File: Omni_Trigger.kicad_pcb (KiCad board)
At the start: 2 copper layers, 127 x 48 mm, 43 parts, among them J1 Conn_02x13_Top_Bottom, J2 Conn_02x04_Odd_Even, J3 Conn_02x02_Odd_Even, J4 Conn_02x04_Odd_Even, J5 Screw_Terminal_01x08, J6 Screw_Terminal_01x04, J7 Screw_Terminal_01x02, J8 Screw_Terminal_01x02, K1 G5LE-1, K2 G5LE-1, K3 G5LE-1, K4 G5LE-1, Q1 BS170F, Q2 BS170F, Q3 BS170F, Q4 BS170F

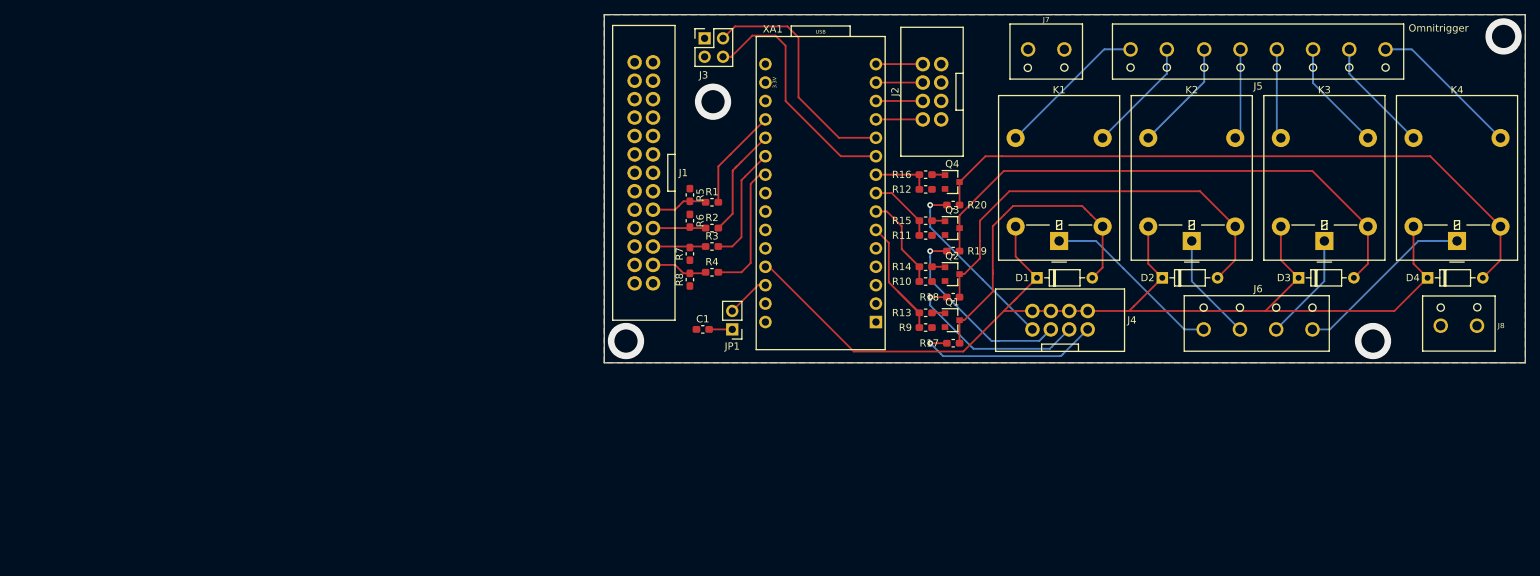
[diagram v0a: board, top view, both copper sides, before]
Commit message: Redrew Board in Stablöe Kicad for compatibility
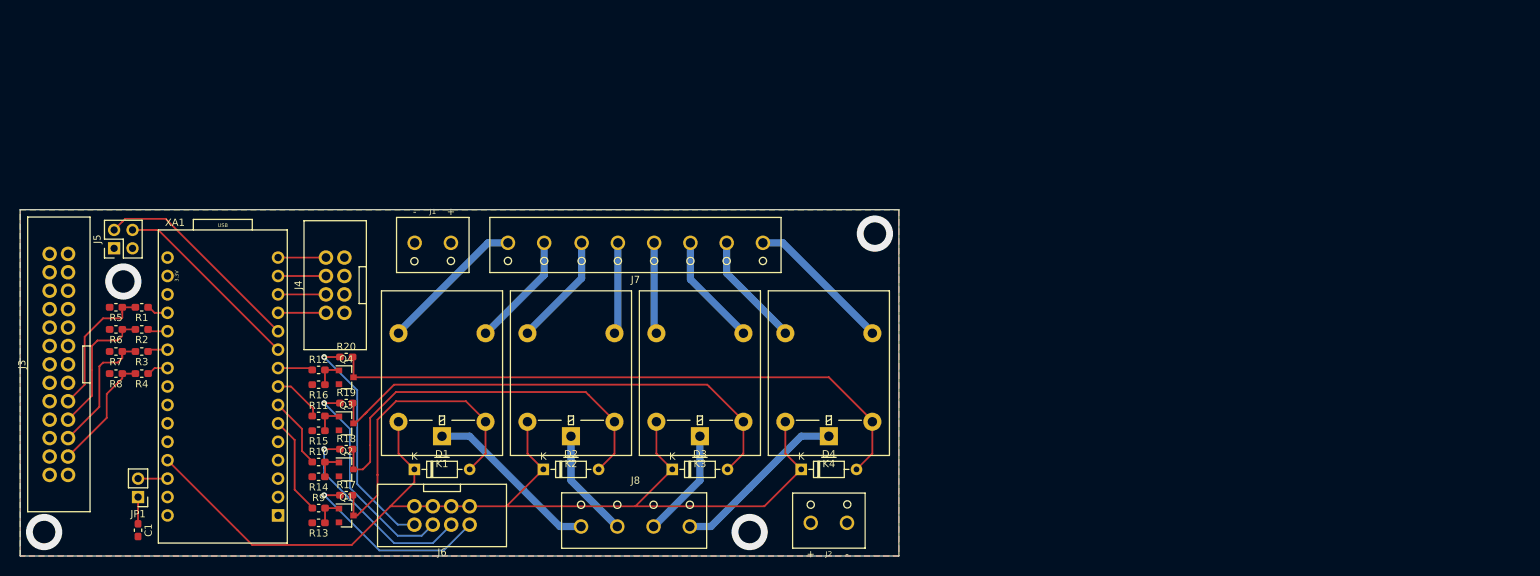
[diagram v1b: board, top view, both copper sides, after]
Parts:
- J1: value Conn_02x13_Top_Bottom -> Screw_Terminal_01x02; footprint IDC:IDC_13x02_Sided -> RS_Screw:RS_Screw_Term_x2
- J2: value Conn_02x04_Odd_Even -> Screw_Terminal_01x02; footprint IDC:IDC_04x02 -> RS_Screw:RS_Screw_Term_x2
- J3: value Conn_02x02_Odd_Even -> Conn_02x13_Top_Bottom; footprint Connector_PinHeader_2.54mm:PinHeader_2x02_P2.54mm_Vertical -> IDC:IDC_13x02_Sided
- J5: value Screw_Terminal_01x08 -> Conn_02x02_Odd_Even; footprint RS_Screw:RS_Screw_Term_x8 -> Connector_PinHeader_2.54mm:PinHeader_2x02_P2.54mm_Vertical
- J6: value Screw_Terminal_01x04 -> Conn_02x04_Odd_Even; footprint RS_Screw:RS_Screw_Term_x4 -> IDC:IDC_04x02
- J7: value Screw_Terminal_01x02 -> Screw_Terminal_01x08; footprint RS_Screw:RS_Screw_Term_x2 -> RS_Screw:RS_Screw_Term_x8
- J8: value Screw_Terminal_01x02 -> Screw_Terminal_01x04; footprint RS_Screw:RS_Screw_Term_x2 -> RS_Screw:RS_Screw_Term_x4
- R1, R13, R14, R15, R16, R2, R3, R4: value 100 -> R
- R10, R11, R12, R5, R6, R7, R8, R9: value 10k -> R
- R17, R18, R19, R20: value 300 -> R
- moved J5 160.1 mm to (42.4, 93.2), turned to 90 degrees
- moved J8 116.9 mm to (114.3, 131.6)
- moved J6 115.4 mm to (87.6, 130.0), turned to 180 degrees
- moved J4 100.1 mm to (72.9, 98.3), turned to 90 degrees
- moved J3 99.7 mm to (34.8, 109.2), turned to 90 degrees
- moved K4 90.7 mm to (141.0, 119.1)
- moved D3 90.3 mm to (119.4, 123.7)
- moved D4 90.3 mm to (137.2, 123.7)
- moved K3 90.2 mm to (123.2, 119.1)
- moved D1 89.8 mm to (83.8, 123.7)
- moved K2 89.7 mm to (105.4, 119.1)
- moved D2 89.3 mm to (101.6, 123.7)
- moved K1 89.2 mm to (87.6, 119.1)
- moved R13 88.6 mm to (70.6, 131.1)
- moved R14 88.6 mm to (70.6, 124.7)
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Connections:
- C1 pad 1: GND -> Net-(C1-Pad1)
- C1 pad 2: Net-(C1-Pad2) -> GND
- J1 pad 1: (no net) -> /Shield
- J1 pad 2: Net-(J1-Pad2) -> /Shield
- J2 pad 1: GND -> /Shield
- J2 pad 2: Net-(J2-Pad2) -> /Shield
- J3 pad 1: GND -> Net-(J3-Pad1)
- J3 pad 3: GND -> Net-(J3-Pad3)
- J4 pad 1: Net-(J4-Pad1) -> GND
- J4 pad 2: +5V -> Net-(J4-Pad2)
- J4 pad 3: Net-(J4-Pad3) -> GND
- J4 pad 4: +5V -> Net-(J4-Pad4)
- J4 pad 5: Net-(J4-Pad5) -> GND
- J4 pad 6: +5V -> Net-(J4-Pad6)
- J4 pad 7: Net-(J4-Pad7) -> GND
- J4 pad 8: +5V -> Net-(J4-Pad8)
- J5 pad 1: Net-(J5-Pad1) -> GND
- J5 pad 3: Net-(J5-Pad3) -> GND
- J6 pad 1: Net-(J6-Pad1) -> +5V
- J6 pad 3: Net-(J6-Pad3) -> +5V
- J7 pad 1: /Shield -> Net-(J7-Pad1)
- J7 pad 2: /Shield -> Net-(J7-Pad2)
- J8 pad 1: /Shield -> Net-(J8-Pad1)
- J8 pad 2: /Shield -> Net-(J8-Pad2)
- JP1 pad 1: Net-(C1-Pad2) -> Net-(C1-Pad1)
- K1 pad 1: Net-(J6-Pad1) -> Net-(J8-Pad1)
- K1 pad 3: Net-(J5-Pad7) -> Net-(J7-Pad7)
- K1 pad 4: Net-(J5-Pad8) -> Net-(J7-Pad8)
- K2 pad 1: Net-(J6-Pad2) -> Net-(J8-Pad2)
- K2 pad 3: Net-(J5-Pad5) -> Net-(J7-Pad5)
- K2 pad 4: Net-(J5-Pad6) -> Net-(J7-Pad6)
- K3 pad 1: Net-(J6-Pad3) -> Net-(J8-Pad3)
- K3 pad 3: Net-(J5-Pad3) -> Net-(J7-Pad3)
- K3 pad 4: Net-(J5-Pad4) -> Net-(J7-Pad4)
- K4 pad 1: Net-(J6-Pad4) -> Net-(J8-Pad4)
- K4 pad 3: Net-(J5-Pad1) -> Net-(J7-Pad1)
- K4 pad 4: Net-(J5-Pad2) -> Net-(J7-Pad2)
- R1 pad 1: Net-(J1-Pad5) -> Net-(R1-Pad1)
- R1 pad 2: Net-(R1-Pad2) -> Net-(J3-Pad5)
- R10 pad 1: GND -> Net-(R10-Pad1)
- R10 pad 2: Net-(R10-Pad2) -> Net-(Q2-Pad1)
- R11 pad 1: GND -> Net-(R11-Pad1)
- R11 pad 2: Net-(R11-Pad2) -> Net-(Q3-Pad1)
- R12 pad 1: GND -> Net-(R12-Pad1)
- R12 pad 2: Net-(R12-Pad2) -> Net-(Q4-Pad1)
- R13 pad 2: Net-(R13-Pad2) -> GND
- R14 pad 2: Net-(R10-Pad2) -> GND
- R15 pad 2: Net-(R11-Pad2) -> GND
- R16 pad 2: Net-(R12-Pad2) -> GND
- R17 pad 1: Net-(J4-Pad7) -> Net-(J6-Pad2)
- R18 pad 1: Net-(J4-Pad5) -> Net-(J6-Pad4)
- R19 pad 1: Net-(J4-Pad3) -> Net-(J6-Pad6)
- R2 pad 1: Net-(J1-Pad4) -> Net-(R2-Pad1)
- R2 pad 2: Net-(R2-Pad2) -> Net-(J3-Pad4)
- R20 pad 1: Net-(J4-Pad1) -> Net-(J6-Pad8)
- R3 pad 1: Net-(J1-Pad3) -> Net-(R3-Pad1)
- R3 pad 2: Net-(R3-Pad2) -> Net-(J3-Pad3)
- R4 pad 1: Net-(J1-Pad2) -> Net-(R4-Pad1)
- R4 pad 2: Net-(R4-Pad2) -> Net-(J3-Pad2)
- R5 pad 1: GND -> Net-(J3-Pad5)
- R5 pad 2: Net-(J1-Pad5) -> GND
- R6 pad 1: GND -> Net-(J3-Pad4)
- R6 pad 2: Net-(J1-Pad4) -> GND
- R7 pad 1: GND -> Net-(J3-Pad3)
- R7 pad 2: Net-(J1-Pad3) -> GND
- R8 pad 1: GND -> Net-(J3-Pad2)
- R8 pad 2: Net-(J1-Pad2) -> GND
- R9 pad 1: GND -> Net-(R9-Pad1)
- R9 pad 2: Net-(R13-Pad2) -> Net-(Q1-Pad1)
- XA1 pad 3V3: (no net) -> Net-(XA1-Pad3V3)
- XA1 pad A0: Net-(R1-Pad2) -> Net-(R1-Pad1)
- XA1 pad A1: Net-(R2-Pad2) -> Net-(R2-Pad1)
- XA1 pad A2: Net-(R3-Pad2) -> Net-(R3-Pad1)
- XA1 pad A3: Net-(R4-Pad2) -> Net-(R4-Pad1)
- XA1 pad A4: (no net) -> Net-(XA1-PadA4)
- XA1 pad A5: (no net) -> Net-(XA1-PadA5)
- XA1 pad A6: (no net) -> Net-(XA1-PadA6)
- XA1 pad A7: (no net) -> Net-(XA1-PadA7)
- XA1 pad AREF: (no net) -> Net-(XA1-PadAREF)
- XA1 pad D0: (no net) -> Net-(XA1-PadD0)
- XA1 pad D1: (no net) -> Net-(XA1-PadD1)
- XA1 pad D10: Net-(J2-Pad4) -> Net-(J4-Pad4)
- XA1 pad D11: Net-(J2-Pad6) -> Net-(J4-Pad6)
- XA1 pad D12: Net-(J2-Pad8) -> Net-(J4-Pad8)
- XA1 pad D13: (no net) -> Net-(XA1-PadD13)
- XA1 pad D2: (no net) -> Net-(XA1-PadD2)
- XA1 pad D3: Net-(R13-Pad2) -> Net-(R9-Pad1)
- XA1 pad D4: Net-(R10-Pad2) -> Net-(R10-Pad1)
- XA1 pad D5: Net-(R11-Pad2) -> Net-(R11-Pad1)
- XA1 pad D6: Net-(R12-Pad2) -> Net-(R12-Pad1)
- XA1 pad D7: Net-(J3-Pad4) -> Net-(J5-Pad4)
- XA1 pad D8: Net-(J3-Pad2) -> Net-(J5-Pad2)
- XA1 pad D9: Net-(J2-Pad2) -> Net-(J4-Pad2)
- XA1 pad RST1: (no net) -> Net-(XA1-PadRST1)
- XA1 pad VIN: (no net) -> Net-(XA1-PadVIN)
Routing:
- net Net-(J6-Pad8): track 0.00 -> 31.8 mm, vias 0 -> 1
- net Net-(J6-Pad6): track 0.00 -> 30.1 mm, vias 0 -> 1
- net Net-(J4-Pad3): track 27.0 -> 0.00 mm, vias 1 -> 0
- net Net-(J4-Pad7): track 26.3 -> 0.00 mm, vias 1 -> 0
- net Net-(J4-Pad5): track 26.2 -> 0.00 mm, vias 1 -> 0
- net Net-(J4-Pad1): track 25.3 -> 0.00 mm, vias 1 -> 0
- net Net-(J6-Pad1): track 25.0 -> 0.00 mm
- net Net-(J8-Pad4): track 0.00 -> 24.5 mm
- net Net-(J8-Pad1): track 0.00 -> 24.5 mm
- net Net-(J5-Pad8): track 20.9 -> 0.00 mm
- net Net-(J5-Pad1): track 20.9 -> 0.00 mm
- net Net-(J7-Pad1): track 0.00 -> 20.3 mm
- net Net-(J7-Pad8): track 0.00 -> 20.3 mm
- net Net-(R13-Pad2): track 20.1 -> 0.00 mm
- net Net-(J3-Pad5): track 0.00 -> 19.5 mm
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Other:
- board size 127 x 48 mm -> 121.2 x 47.8 mm
- net class Signal added: clearance 0.2, trace_width 1, via_dia 0.8, via_drill 0.4
- board text removed: "Omnitrigger"

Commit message: Made ground connection to shield plane available at screw terminals
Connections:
- J1 pad 1: /Shield -> GND
- J2 pad 1: /Shield -> GND
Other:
- board text added: "G"
- board text added: "S"

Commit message: Updated clearances
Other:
- net class Default: clearance 0.2 -> 0.15
- net class Signal: clearance 0.2 -> 0.65
- rule trace_clearance: 0.2 -> 0.15
